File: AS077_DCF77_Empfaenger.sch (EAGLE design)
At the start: 81 parts, among them IC1 4093N, IC2 4538N, IC3 CA3130E, IC4 4093N, J1 Rückkopplung, J2 JUMPER_J5MM, J3 JUMPER_J5MM, Q1 BF244A, Q2 BC549C, Q3 BC549C, Q4 BC549C, Q5 BC549C, Q6 BC559C, Q7 BC549C

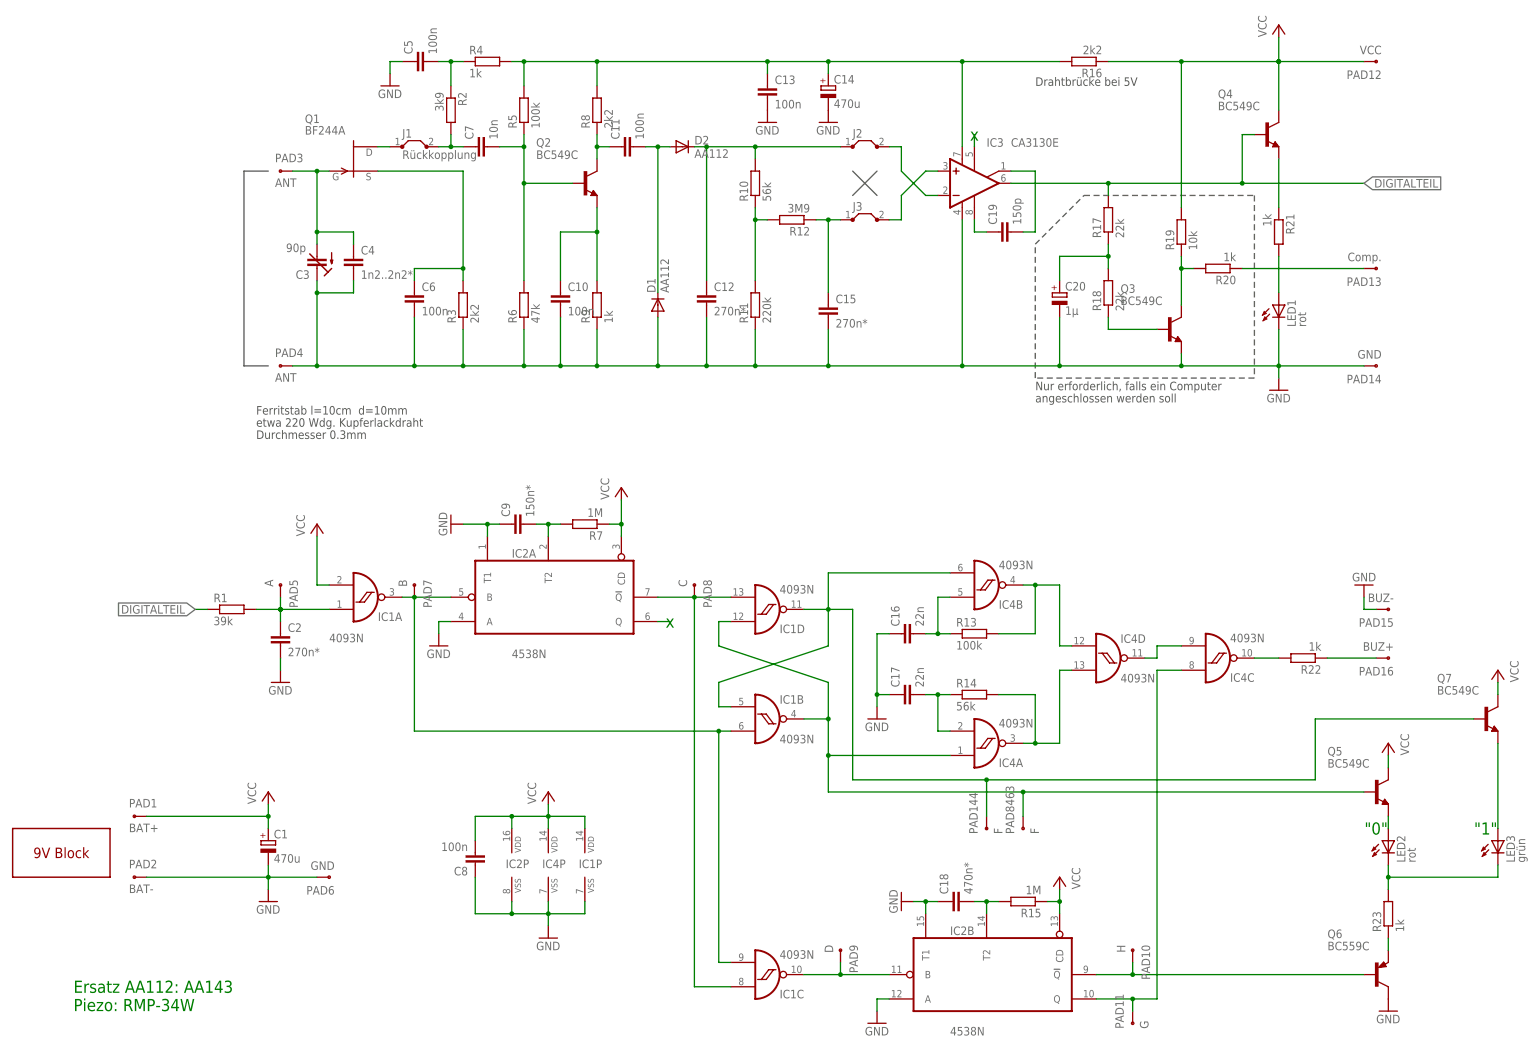
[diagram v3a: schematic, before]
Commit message: * Updated and cleaned up the library * Cleaned up the schematic * Renumbered all parts * Updated images, gerbers and schematic pdf * Added small arduino test script for decoding
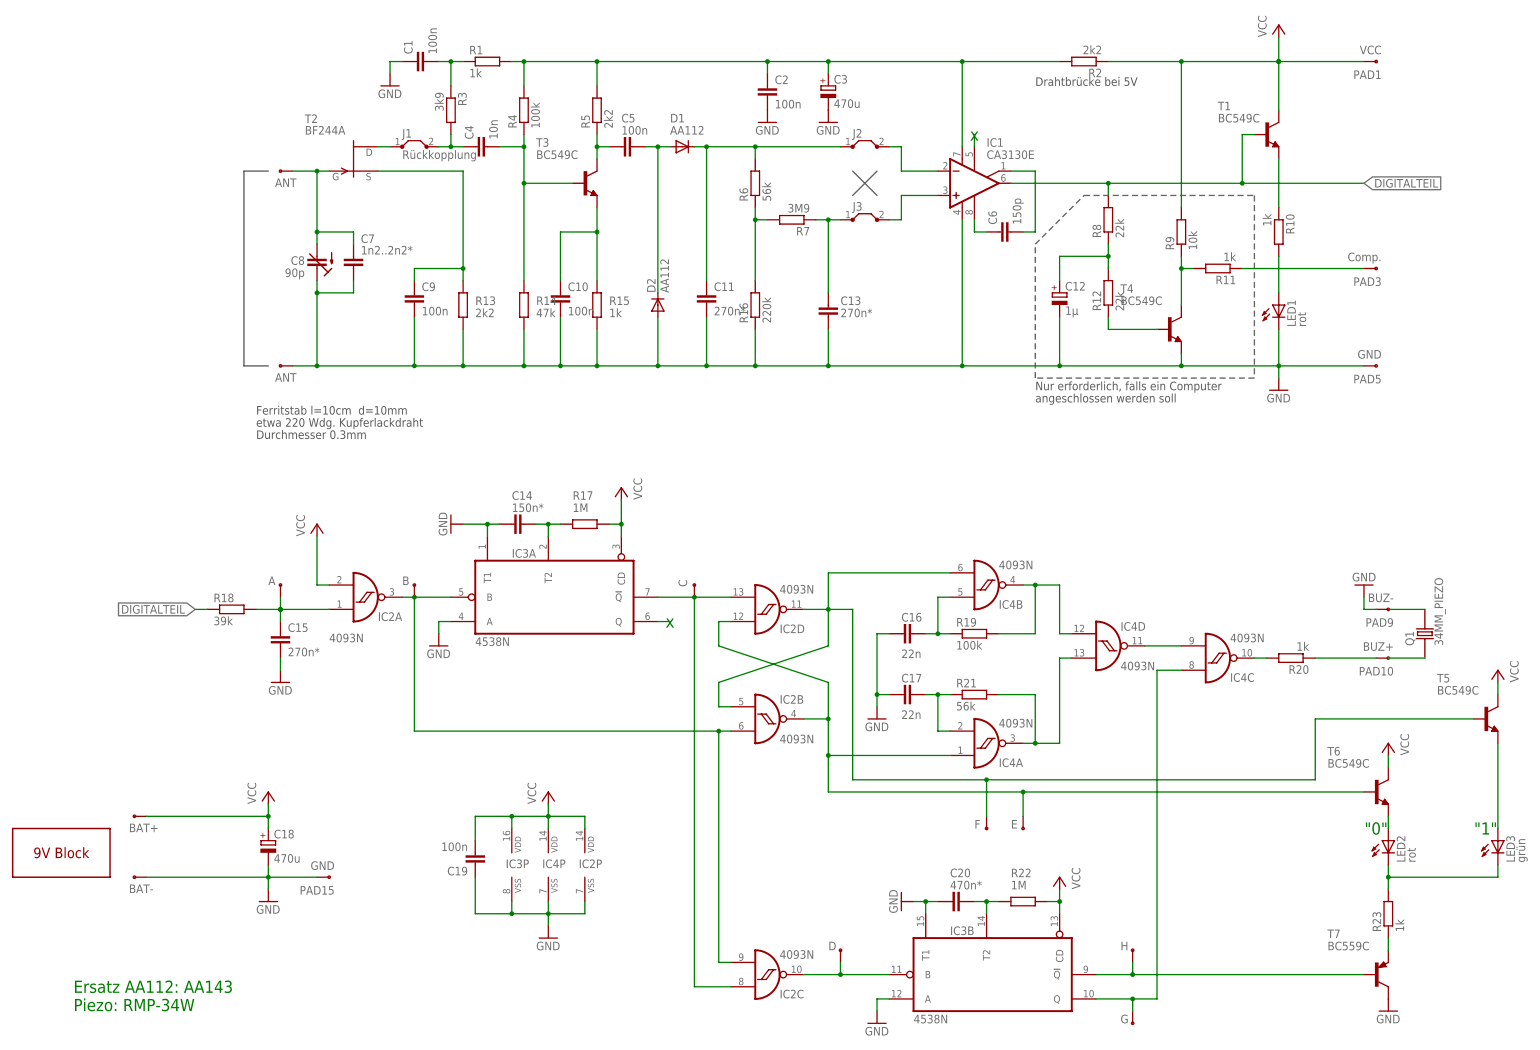
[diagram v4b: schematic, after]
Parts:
- removed PAD144, PAD8463: F, 0027 DCF77-Empfänger:WIREPAD_2.2/1.3
- removed Q2, Q3, Q4: BC549C, 0027 DCF77-Empfänger:TRANSISTOR-NPN_BC2385.08
- removed Q5, Q7: BC549C, 0027 DCF77-Empfänger:TRANSISTOR-NPN_BC2382.54
- removed Q6: BC559C, 0027 DCF77-Empfänger:TRANSISTOR-PNP_BC2145.08
- added PAD17: H, 0027 DCF77-Empfänger:WIREPAD_2.2/1.3
- added PAD18: G, 0027 DCF77-Empfänger:WIREPAD_2.2/1.3
- added T1, T3, T4: BC549C, 0027 DCF77-Empfänger:BC549C5.08
- added T2: BF244A, 0027 DCF77-Empfänger:BF244A5.08
- added T5, T6: BC549C, 0027 DCF77-Empfänger:BC549C2.54
- added T7: BC559C, 0027 DCF77-Empfänger:BC559C5.08
- C1: value 470u -> 100n; device 0027 DCF77-Empfänger:RCL_CPOL-EUE5-10.5 -> 0027 DCF77-Empfänger:RCL_C-EU050-024X044
- C11, C13: value 100n -> 270n*; device 0027 DCF77-Empfänger:RCL_C-EU050-024X044 -> 0027 DCF77-Empfänger:RCL_C-EU075-032X103
- C12: value 270n* -> 1µ; device 0027 DCF77-Empfänger:RCL_C-EU075-032X103 -> 0027 DCF77-Empfänger:RCL_CPOL-EUE5-6
- C14: value 470u -> 150n*; device 0027 DCF77-Empfänger:RCL_CPOL-EUE5-10.5 -> 0027 DCF77-Empfänger:RCL_C-EU075-032X103
- C18: value 470n* -> 470u; device 0027 DCF77-Empfänger:RCL_C-EU075-032X103 -> 0027 DCF77-Empfänger:RCL_CPOL-EUE5-10.5
- C19: value 150p -> 100n
- C2: value 270n* -> 100n; device 0027 DCF77-Empfänger:RCL_C-EU075-032X103 -> 0027 DCF77-Empfänger:RCL_C-EU050-024X044
- C20: value 1µ -> 470n*; device 0027 DCF77-Empfänger:RCL_CPOL-EUE5-6 -> 0027 DCF77-Empfänger:RCL_C-EU075-032X103
- C3: value 90p -> 470u; device 0027 DCF77-Empfänger:RCL_C-TRIMM808-7.5 -> 0027 DCF77-Empfänger:RCL_CPOL-EUE5-10.5
- C4: value 1n2..2n2* -> 10n; device 0027 DCF77-Empfänger:RCL_C-EU075-032X103 -> 0027 DCF77-Empfänger:RCL_C-EU050-024X044
- C6: value 100n -> 150p
- C7: value 10n -> 1n2..2n2*; device 0027 DCF77-Empfänger:RCL_C-EU050-024X044 -> 0027 DCF77-Empfänger:RCL_C-EU075-032X103
- C8: value 100n -> 90p; device 0027 DCF77-Empfänger:RCL_C-EU050-024X044 -> 0027 DCF77-Empfänger:RCL_C-TRIMM808-7.5
- C9: value 150n* -> 100n; device 0027 DCF77-Empfänger:RCL_C-EU075-032X103 -> 0027 DCF77-Empfänger:RCL_C-EU050-024X044
- IC1: value 4093N -> CA3130E; device 0027 DCF77-Empfänger:40XX_4093N -> 0027 DCF77-Empfänger:CA3130N
- IC2: value 4538N -> 4093N; device 0027 DCF77-Empfänger:45XX_4538N -> 0027 DCF77-Empfänger:40XX_4093N
- IC3: value CA3130E -> 4538N; device 0027 DCF77-Empfänger:LINEAR_CA3130N -> 0027 DCF77-Empfänger:45XX_4538N
- PAD1: value BAT+ -> VCC
- PAD10: value H -> BUZ+
- PAD11: value G -> BAT+
- PAD12: value VCC -> F
- PAD13: value Comp. -> E
- PAD14: value GND -> BAT-
- PAD15: value BUZ- -> GND
- PAD16: value BUZ+ -> D
- PAD2: value BAT- -> ANT
- PAD3: value ANT -> Comp.
- PAD5: value A -> GND
- PAD6: value GND -> A
- PAD9: value D -> BUZ-
- Q1: value BF244A -> 34MM_PIEZO; device 0027 DCF77-Empfänger:TRANSISTOR-FET_BF2455.08 -> 0027 DCF77-Empfänger:34MM_PIEZO
- R1: value 39k -> 1k; device 0027 DCF77-Empfänger:RCL_R-EU_0207/15 -> 0027 DCF77-Empfänger:RCL_R-EU_0207/5V
- R10: value 56k -> 1k
- R11: value 220k -> 1k
- R12: value 3M9 -> 22k
- R13, R5: value 100k -> 2k2
- R14: value 56k -> 47k
- R15: value 1M -> 1k; device 0027 DCF77-Empfänger:RCL_R-EU_0207/15 -> 0027 DCF77-Empfänger:RCL_R-EU_0207/5V
- R16: value 2k2 -> 220k
- R17: value 22k -> 1M; device 0027 DCF77-Empfänger:RCL_R-EU_0207/5V -> 0027 DCF77-Empfänger:RCL_R-EU_0207/15
- R18: value 22k -> 39k; device 0027 DCF77-Empfänger:RCL_R-EU_0207/5V -> 0027 DCF77-Empfänger:RCL_R-EU_0207/15
- R19: value 10k -> 100k
- R2: value 3k9 -> 2k2; device 0027 DCF77-Empfänger:RCL_R-EU_0207/15 -> 0027 DCF77-Empfänger:RCL_R-EU_0207/5V
- R21: value 1k -> 56k
- R22: value 1k -> 1M; device 0027 DCF77-Empfänger:RCL_R-EU_0207/5V -> 0027 DCF77-Empfänger:RCL_R-EU_0207/15
- R3: value 2k2 -> 3k9; device 0027 DCF77-Empfänger:RCL_R-EU_0207/5V -> 0027 DCF77-Empfänger:RCL_R-EU_0207/15
- R4: value 1k -> 100k
- R6: value 47k -> 56k
- R7: value 1M -> 3M9; device 0027 DCF77-Empfänger:RCL_R-EU_0207/15 -> 0027 DCF77-Empfänger:RCL_R-EU_0207/5V
- R8: value 2k2 -> 22k
- R9: value 1k -> 10k
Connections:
- net DIGITALTEIL: now also IC1.OUT, R18.1, R8.2, T1.B; no longer IC3.OUT, Q4.B, R1.1, R17.2
- net GND: now also C1.1, C11.2, C12.-, C14.1, C18.-, C19.1, C20.1, C3.-, C7.2, C8.E, C9.2, D2.A, IC1.V-, IC3A.A, IC3A.T1, IC3B.A, IC3B.T1, IC3P.VSS, PAD5.P, PAD9.P, R13.1, R14.1, R15.1, R16.1, T4.E, T7.C; no longer C1.-, C12.2, C14.-, C18.1, C20.-, C3.E, C4.2, C5.1, C6.2, C8.1, C9.1, D1.A, IC1P.VSS, IC2A.A, IC2A.T1, IC2B.A, IC2B.T1, IC3.V-, PAD2.P, PAD6.P, Q3.E, Q6.C, R11.1, R3.1, R6.1, R9.1
- net N$1: now also IC1.+IN; no longer IC3.+IN
- net N$10: now also C4.2, R14.2, R4.1, T3.B; no longer C7.2, Q2.B, R5.1, R6.2
- net N$11: now also C2.1, C3.+, IC1.V+, R1.2, R2.2; no longer C13.1, C14.+, IC3.V+, R16.2, R8.2
- net N$12: now also C1.2, R1.1, R3.1; no longer C5.2, R2.1, R4.1
- net N$13: now also C4.1, R3.2; no longer C7.1, R2.2
- net N$14: now also T2.D; no longer Q1.D
- net N$15: now also C9.1, R13.2, T2.S; no longer C6.1, Q1.S, R3.2
- net N$16: now also C6.2, IC1.ON/CMP; no longer C19.2, IC3.ON/CMP
- net N$17: now also PAD10.P, R20.1; no longer PAD16.P, R22.1
- net N$18: now also C7.1, C8.A, PAD2.P, T2.G; no longer C3.A, C4.1, PAD3.P, Q1.G
- net N$19: now also C20.2, IC3B.T2, R22.2; no longer C18.2, IC2B.T2, R15.2
- net N$2: now also IC1.-IN; no longer IC3.-IN
- net N$20: now also C12.+, R12.2, R8.1; no longer C20.+, R17.1, R18.2
- net N$21: now also PAD3.P, R11.1; no longer PAD13.P, R20.1
- net N$22: now also R12.1, T4.B; no longer Q3.B, R18.1
- net N$23: now also R11.2, R9.1, T4.C; no longer Q3.C, R19.1, R20.2
- net N$24: now also R10.2; no longer R21.2
- net N$25: now also R10.1, T1.E; no longer Q4.E, R21.1
- net N$26: now also C15.1, IC2A.I0, PAD6.P, R18.2; no longer C2.1, IC1A.I0, PAD5.P, R1.2
- net N$27: now also IC2C.I0, IC2D.I1, IC3A.!Q; no longer IC1C.I0, IC1D.I1, IC2A.!Q
- net N$28: now also IC2B.I0, IC2D.O, PAD12.P, T5.B; no longer IC1B.I0, IC1D.O, PAD144.P, Q7.B
- net N$29: now also R19.2; no longer R13.2
- net N$3: now also C13.1, R7.1; no longer C15.1, R12.1
- net N$30: now also IC2A.O, IC2B.I1, IC2C.I1, IC3A.B; no longer IC1A.O, IC1B.I1, IC1C.I1, IC2A.B
- net N$31: now also IC2C.O, IC3B.B, PAD16.P; no longer IC1C.O, IC2B.B, PAD9.P
- net N$32: now also IC2B.O, IC2D.I0, PAD13.P, T6.B; no longer IC1B.O, IC1D.I0, PAD8463.P, Q5.B
- net N$33: now also R21.2; no longer R14.2
- net N$35: now also R19.1; no longer R13.1
- net N$36: now also R21.1; no longer R14.1
- net N$37: now also C14.2, IC3A.T2, R17.2; no longer C9.2, IC2A.T2, R7.2
- net N$38: now also IC3B.Q, PAD18.P; no longer IC2B.Q, PAD11.P
- net N$39: now also IC3B.!Q, PAD17.P, T7.B; no longer IC2B.!Q, PAD10.P, Q6.B
- net N$4: now also R16.2, R6.1, R7.2; no longer R10.1, R11.2, R12.2
- net N$40: now also T7.E; no longer Q6.E
- net N$41: now also T6.E; no longer Q5.E
- net N$42: now also T5.E; no longer Q7.E
- net N$44: now also R20.2; no longer R22.2
- net N$45: now also IC3A.Q; no longer IC2A.Q
- net N$46: now also IC1.ON; no longer IC3.ON
- net N$5: now also C11.1, D1.C, R6.2; no longer C12.1, D2.C, R10.2
- net N$6: now also C5.2, D1.A, D2.C; no longer C11.2, D1.C, D2.A
- net N$7: now also C6.1, IC1.CMP; no longer C19.1, IC3.CMP
- net N$8: now also R15.2, T3.E; no longer Q2.E, R9.2
- net N$9: now also C5.1, R5.1, T3.C; no longer C11.1, Q2.C, R8.1
- net VCC: now also C18.+, C19.2, IC2A.I1, IC3A.CD, IC3B.CD, IC3P.VDD, PAD11.P, R17.1, R2.1, R22.1, R9.2, T1.C, T5.C, T6.C; no longer C1.+, C8.2, IC1A.I1, IC1P.VDD, IC2A.CD, IC2B.CD, PAD12.P, Q4.C, Q5.C, Q7.C, R15.1, R16.1, R19.2, R7.1
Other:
- moved on the sheet: C11, C13, C15, C19, C2, C4, C5, C6, C7, C9, D1, D2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
